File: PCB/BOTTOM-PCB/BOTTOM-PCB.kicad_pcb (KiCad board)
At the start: 2 copper layers, 61 x 61 mm, 8 parts, among them J1 Conn_01x10_Pin, J2 Conn_01x03_Pin, J3 Conn_01x02_Pin, U1 MLX90393SLW-ABA-011-RE

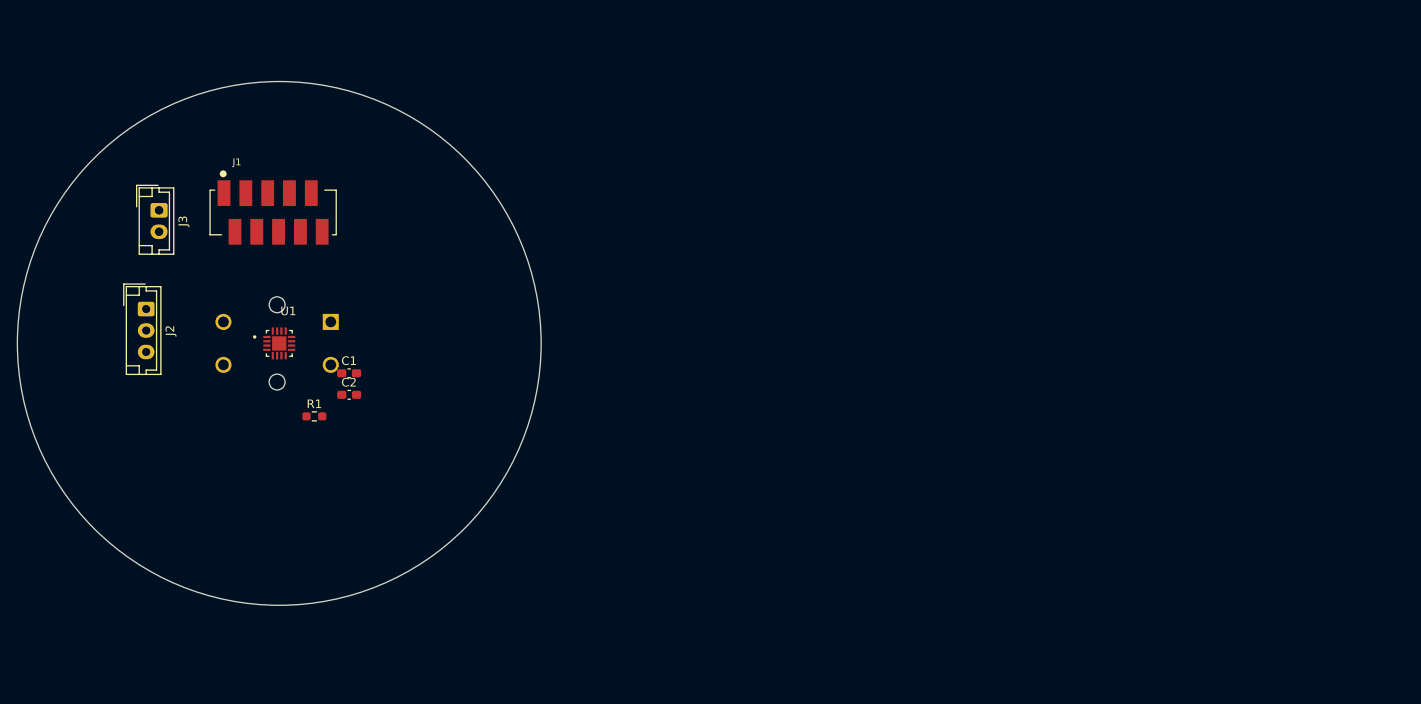
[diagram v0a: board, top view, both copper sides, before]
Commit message: re organization of top and bottom pcb
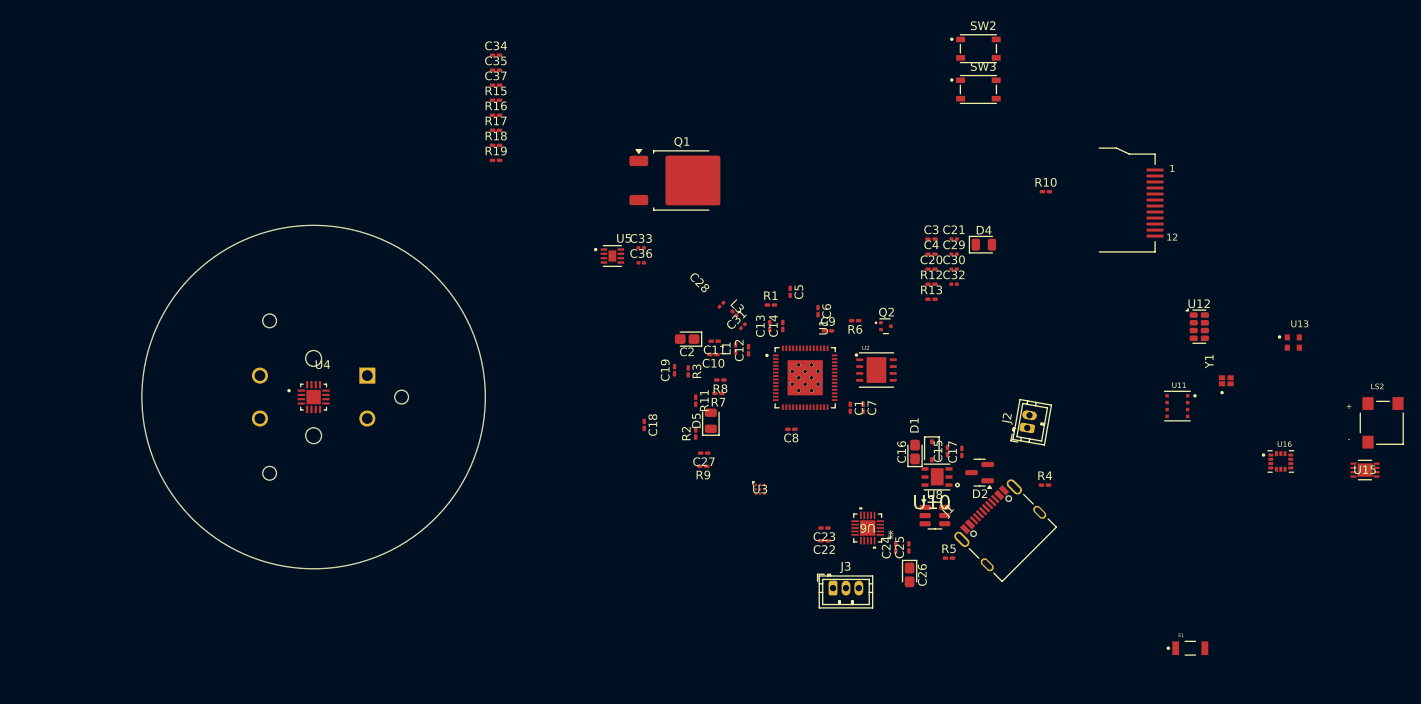
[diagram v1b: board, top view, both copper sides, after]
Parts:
- added C10: 0.1 uF, Capacitor_SMD:C_0201_0603Metric_Pad0.64x0.40mm_HandSolder, F.Cu at (189.1, 79.8)
- added C11: 1 uF, Capacitor_SMD:C_0201_0603Metric_Pad0.64x0.40mm_HandSolder, F.Cu at (189.2, 78.2)
- added C12: 0.1 uF, Capacitor_SMD:C_0201_0603Metric_Pad0.64x0.40mm_HandSolder, F.Cu at (193.2, 79.3)
- added C13: 10 nF, Capacitor_SMD:C_0201_0603Metric_Pad0.64x0.40mm_HandSolder, F.Cu at (195.6, 76.5)
- added C14: 1 uF, Capacitor_SMD:C_0201_0603Metric_Pad0.64x0.40mm_HandSolder, F.Cu at (197.1, 76.5)
- added C15: 1 uF, Capacitor_SMD:C_0201_0603Metric_Pad0.64x0.40mm_HandSolder, F.Cu at (216.3, 91.0)
- added C16: 10 uF, Capacitor_Tantalum_SMD:CP_EIA-1608-08_AVX-J_HandSolder, F.Cu at (212.5, 91.1)
- added C17: 1 uF, Capacitor_SMD:C_0201_0603Metric_Pad0.64x0.40mm_HandSolder, F.Cu at (218.0, 91.1)
- added C18: 0.1 uF, Capacitor_SMD:C_0201_0603Metric_Pad0.64x0.40mm_HandSolder, F.Cu at (181.0, 88.0)
- added C19: 0.1 uF, Capacitor_SMD:C_0201_0603Metric_Pad0.64x0.40mm_HandSolder, F.Cu at (184.5, 81.6)
- added C20: 0.1 uF, Capacitor_SMD:C_0201_0603Metric_Pad0.64x0.40mm_HandSolder, F.Cu at (214.5, 69.9)
- added C21: 1 uF, Capacitor_SMD:C_0201_0603Metric, F.Cu at (217.1, 66.4)
- added C22: 0.1 uF, Capacitor_SMD:C_0201_0603Metric_Pad0.64x0.40mm_HandSolder, F.Cu at (202.0, 101.5)
- added C23: 0.1 uF, Capacitor_SMD:C_0201_0603Metric_Pad0.64x0.40mm_HandSolder, F.Cu at (202.0, 100.0)
- added C24: 0.1 uF, Capacitor_SMD:C_0201_0603Metric_Pad0.64x0.40mm_HandSolder, F.Cu at (210.3, 102.3)
- added C25: 0.1 uF, Capacitor_SMD:C_0201_0603Metric_Pad0.64x0.40mm_HandSolder, F.Cu at (211.8, 102.3)
- added C26: 22 uF, Capacitor_Tantalum_SMD:CP_EIA-1608-08_AVX-J_HandSolder, F.Cu at (211.9, 105.5)
- added C27: 0.1 uF, Capacitor_SMD:C_0201_0603Metric_Pad0.64x0.40mm_HandSolder, F.Cu at (188.0, 91.3)
- added C28: 1.8 pF, Capacitor_SMD:C_0201_0603Metric, F.Cu at (190.0, 74.0)
- added C29: 1 uF, Capacitor_SMD:C_0201_0603Metric, F.Cu at (217.1, 68.1)
- added C3: 0.1 uF, Capacitor_SMD:C_0201_0603Metric_Pad0.64x0.40mm_HandSolder, F.Cu at (214.5, 66.4)
- added C30: 4.7 uF, Capacitor_SMD:C_0201_0603Metric, F.Cu at (217.1, 69.9)
- added C31: 1.5 pF, Capacitor_SMD:C_0201_0603Metric, F.Cu at (192.5, 76.5)
- added C32: 4.7 uF, Capacitor_SMD:C_0201_0603Metric, F.Cu at (217.1, 71.6)
- added C33: 0.1 uF, Capacitor_SMD:C_0201_0603Metric, F.Cu at (180.7, 67.4)
- added C34: 0.1 uF, Capacitor_SMD:C_0201_0603Metric_Pad0.64x0.40mm_HandSolder, F.Cu at (163.7, 44.9)
- added C35: 22 uF, Capacitor_SMD:C_0201_0603Metric_Pad0.64x0.40mm_HandSolder, F.Cu at (163.7, 46.7)
- added C36: 0.1 uF, Capacitor_SMD:C_0201_0603Metric, F.Cu at (180.7, 69.1)
- added C37: 0.1 uF, Capacitor_SMD:C_0201_0603Metric_Pad0.64x0.40mm_HandSolder, F.Cu at (163.7, 48.4)
- added C4: 0.1 uF, Capacitor_SMD:C_0201_0603Metric_Pad0.64x0.40mm_HandSolder, F.Cu at (214.5, 68.1)
- added C5: 6 pF, Capacitor_SMD:C_0201_0603Metric_Pad0.64x0.40mm_HandSolder, F.Cu at (198.0, 72.5)
- added C6: 6 pF, Capacitor_SMD:C_0201_0603Metric_Pad0.64x0.40mm_HandSolder, F.Cu at (201.2, 74.7)
- added C7: 0.1 uF, Capacitor_SMD:C_0201_0603Metric_Pad0.64x0.40mm_HandSolder, F.Cu at (206.5, 86.0)
- added C8: 0.1 uF, Capacitor_SMD:C_0201_0603Metric_Pad0.64x0.40mm_HandSolder, F.Cu at (198.1, 88.5)
- added C9: 0.1 uF, Capacitor_SMD:C_0201_0603Metric_Pad0.64x0.40mm_HandSolder, F.Cu at (202.4, 77.0)
- added D1: SD03_SOD323, Diode_SMD:D_SOD-323, F.Cu at (214.5, 91.0)
- added D2: BAT54C, Package_TO_SOT_SMD:SOT-23, F.Cu at (220.1, 93.5)
- added D4: LED, LED_SMD:LED_0805_2012Metric, F.Cu at (220.6, 67.0)
- added D5: LED, LED_SMD:LED_0805_2012Metric, F.Cu at (188.8, 87.5)
- added E1: AMCA31-2R450G-S1F-T3, AMCA31_2R450G_S1F_T3:XDCR_AMCA31-2R450G-S1F-T3, F.Cu at (244.6, 114.0)
- added J5: Conn_01x12_Pin, GC9A01:GC9A01Round1.28, F.Cu at (240.5, 62.1)
- added L1: 2.0 nH, Inductor_SMD:L_0201_0603Metric_Pad0.64x0.40mm_HandSolder, F.Cu at (191.7, 79.1)
- added L3: 3.9 nH, Inductor_SMD:L_0201_0603Metric, F.Cu at (191.5, 75.0)
- added LS2: CMT-0525-75-SMT-TR, CMT_0525_75_SMT_TR:XDCR_CMT-0525-75-SMT-TR, F.Cu at (266.9, 87.8)
- added Q1: QM6006D, Package_TO_SOT_SMD:TO-252-2, F.Cu at (185.4, 59.5)
- added Q2: NPN, Package_TO_SOT_SMD:SOT-723, F.Cu at (209.2, 76.5)
- added R10: 10 K, Resistor_SMD:R_0201_0603Metric_Pad0.64x0.40mm_HandSolder, F.Cu at (227.8, 60.8)
- added R11: 220, Resistor_SMD:R_0201_0603Metric_Pad0.64x0.40mm_HandSolder, F.Cu at (187.0, 85.2)
- added R12: 470, Resistor_SMD:R_0201_0603Metric_Pad0.64x0.40mm_HandSolder, F.Cu at (214.5, 71.6)
- added R13: 2k, Resistor_SMD:R_0201_0603Metric_Pad0.64x0.40mm_HandSolder, F.Cu at (214.5, 73.4)
- added R15: 10 K, Resistor_SMD:R_0201_0603Metric_Pad0.64x0.40mm_HandSolder, F.Cu at (163.7, 50.2)
- added R16: 10 K, Resistor_SMD:R_0201_0603Metric_Pad0.64x0.40mm_HandSolder, F.Cu at (163.7, 51.9)
- added R17: 1 M, Resistor_SMD:R_0201_0603Metric_Pad0.64x0.40mm_HandSolder, F.Cu at (163.7, 53.7)
- added R18: 22R, Resistor_SMD:R_0201_0603Metric_Pad0.64x0.40mm_HandSolder, F.Cu at (163.7, 55.4)
- added R19: 5 K, Resistor_SMD:R_0201_0603Metric_Pad0.64x0.40mm_HandSolder, F.Cu at (163.7, 57.2)
- added R2: 5 K, Resistor_SMD:R_0201_0603Metric_Pad0.64x0.40mm_HandSolder, F.Cu at (187.0, 89.0)
- added R3: 5 K, Resistor_SMD:R_0201_0603Metric_Pad0.64x0.40mm_HandSolder, F.Cu at (186.1, 81.8)
- added R4: 5 K, Resistor_SMD:R_0201_0603Metric_Pad0.64x0.40mm_HandSolder, F.Cu at (227.7, 95.0)
- added R5: 5 K, Resistor_SMD:R_0201_0603Metric_Pad0.64x0.40mm_HandSolder, F.Cu at (216.5, 103.5)
- added R6: 5 K, Resistor_SMD:R_0201_0603Metric_Pad0.64x0.40mm_HandSolder, F.Cu at (205.6, 75.9)
- added R7: 10 K, Resistor_SMD:R_0201_0603Metric_Pad0.64x0.40mm_HandSolder, F.Cu at (189.6, 84.3)
- added R8: 10 K, Resistor_SMD:R_0201_0603Metric_Pad0.64x0.40mm_HandSolder, F.Cu at (189.9, 82.8)
- added R9: 10 K, Resistor_SMD:R_0201_0603Metric_Pad0.64x0.40mm_HandSolder, F.Cu at (187.9, 92.8)
- added SW2: PTS810_SJM_250_SMTR_LFS, PTS810SJM250SMTR_LFS:SW_PTS810_SJM_250_SMTR_LFS, F.Cu at (219.9, 44.2)
- added SW3: PTS810_SJM_250_SMTR_LFS, PTS810SJM250SMTR_LFS:SW_PTS810_SJM_250_SMTR_LFS, F.Cu at (219.9, 48.9)
- added U10: LP38691SD-3.3, LP38691SD_3_3_NOPB:DFN300X300X80-7N, F.Cu at (215.1, 94.1)
- added U11: BME688, BME688:IC_BME688, F.Cu at (243.1, 85.8)
- added U12: RV-3028-C7_32.768KHZ_1PPM-TA-QC, Package_SON:MicroCrystal_C7_SON-8_1.5x3.2mm_P0.9mm, F.Cu at (245.7, 76.5)
- added U13: LTR-329ALS-01, LTR_329ALS_01:IC_LTR-329ALS-01, F.Cu at (256.6, 78.4)
- added U15: MCP73832T-2ACI/MC, MCP73832T:DFN8_2x3MC_MCH-L, F.Cu at (265.0, 93.2)
- added U16: LSM6DSO32TR, LSM6DSO32TR:XDCR_LSM6DSO32TR, F.Cu at (255.1, 92.2)
- added U2: MX25R6435FZAIH0, MX25R6435FZAIH0:SON80P400X400X60-9N, F.Cu at (208.1, 81.6)
- added U3: DRV2605LYZFR, DRV2605LYZFR:YZF0009ADAD, F.Cu at (194.5, 95.5)
- added U4: MLX90393SLW-ABA-011-RE, MLX90393SLW_ABA_011_RE:QFN50P300X300X100-17N, F.Cu at (142.5, 84.8)
- added U5: MAX17048G_T10, MAX17048G_T10:SON50P200X200X80-9N, F.Cu at (177.3, 68.3)
- added U6: TMC6300-LA-T, tcm6300:21-100586_K2033&plus_1C_ADI-M, F.Cu at (207.0, 100.0)
- added U8: USBLC6-2SC6, Package_TO_SOT_SMD:SOT-23-6, F.Cu at (214.9, 98.5)
- added Y1: ABM12W-40.0000MHZ-8-B1U-T3, ABM12W_40_0000MHZ_8_B1U_T3:XTAL_ABM12W-40.0000MHZ-8-B1U-T3, F.Cu at (248.8, 82.8)
- C1: value 0.1uF -> 1 uF; footprint Capacitor_SMD:C_0603_1608Metric_Pad1.08x0.95mm_HandSolder -> Capacitor_SMD:C_0201_0603Metric_Pad0.64x0.40mm_HandSolder
- C2: value 0.1uF -> 10 uF; footprint Capacitor_SMD:C_0603_1608Metric_Pad1.08x0.95mm_HandSolder -> Capacitor_Tantalum_SMD:CP_EIA-1608-08_AVX-J_HandSolder
- J1: value Conn_01x10_Pin -> 12402012E212A; footprint 8_188275_0:TE_8-188275-0 -> 12402012E212A:AMPHENOL_12402012E212A
- J2: value Conn_01x03_Pin -> S2B-PH-K-SLFSN; footprint Connector_JST:JST_EH_B3B-EH-A_1x03_P2.50mm_Vertical -> Connector_JST:JST_ZH_B2B-ZR_1x02_P1.50mm_Vertical
- J3: value Conn_01x02_Pin -> Conn_01x03_Pin; footprint Connector_JST:JST_EH_B2B-EH-A_1x02_P2.50mm_Vertical -> Connector_JST:JST_ZH_B3B-ZR_1x03_P1.50mm_Vertical
- R1: value 5K -> 0; footprint Resistor_SMD:R_0603_1608Metric_Pad0.98x0.95mm_HandSolder -> Resistor_SMD:R_0201_0603Metric_Pad0.64x0.40mm_HandSolder
- U1: value MLX90393SLW-ABA-011-RE -> ESP32-S3; footprint MLX90393SLW_ABA_011_RE:QFN50P300X300X100-17N -> ESP32_S3:IC_ESP32-S3
- moved J2 103.5 mm to (225.6, 88.3), turned to 80 degrees
- moved J1 94.2 mm to (224.0, 101.2), turned to 45 degrees
- moved J3 90.0 mm to (203.0, 107.0), turned to 0 degrees
- moved U1 61.4 mm to (199.8, 82.5)
- moved C1 58.5 mm to (205.0, 86.0), turned to -90 degrees
- moved R1 54.7 mm to (195.7, 74.0)
- moved C2 39.9 mm to (186.0, 78.0), turned to 180 degrees
- moved S1 7.56 mm to (142.5, 84.8)
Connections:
- C1 pad 1: USR_BUTT -> VDD_SPI
- C2 pad 1: +3V3 -> +3.3V
- J2 pad 1: U -> +BATT
- J2 pad 2: V -> GND
- J3 pad 1: GND -> U
- J3 pad 2: +BATT -> V
- R1 pad 1: +3V3 -> Net-(C5-Pad2)
- R1 pad 2: USR_BUTT -> XTAL_P
- U1 pad 1: GND -> LNA_IN
- U1 pad 10: unconnected-(U1-N/C__2-Pad10) -> Haptic
- U1 pad 11: GND -> VL
- U1 pad 12: GND -> WL
- U1 pad 13: GND -> UL
- U1 pad 14: unconnected-(U1-N/C__3-Pad14) -> WH
- U1 pad 15: +3V3 -> VH
- U1 pad 16: unconnected-(U1-N/C__4-Pad16) -> UH
- U1 pad 17: unconnected-(U1-EXP-Pad17) -> DIAG
- U1 pad 2: ENCODER -> +3.3VA
- U1 pad 3: SCLK -> +3.3VA
- U1 pad 4: unconnected-(U1-N/C-Pad4) -> Reset
- U1 pad 5: DO -> Boot
- U1 pad 6: DO -> LED
- U1 pad 7: GND -> SCL
- U1 pad 8: +3V3 -> SDA
- U1 pad 9: unconnected-(U1-N/C__1-Pad9) -> MFP
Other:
- board size 61 x 61 mm -> 40 x 40 mm

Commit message: start routing on bottom pcb
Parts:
- removed C34: 0.1 uF, Capacitor_SMD:C_0201_0603Metric_Pad0.64x0.40mm_HandSolder
- removed C35: 22 uF, Capacitor_SMD:C_0201_0603Metric_Pad0.64x0.40mm_HandSolder
- removed Q1: QM6006D, Package_TO_SOT_SMD:TO-252-2
- removed R16: 10 K, Resistor_SMD:R_0201_0603Metric_Pad0.64x0.40mm_HandSolder
- removed R17: 1 M, Resistor_SMD:R_0201_0603Metric_Pad0.64x0.40mm_HandSolder
- removed R18: 22R, Resistor_SMD:R_0201_0603Metric_Pad0.64x0.40mm_HandSolder
- added J4: Conn_01x04_Pin, Connector_PinHeader_1.27mm:PinHeader_1x04_P1.27mm_Vertical, F.Cu at (164.2, 63.2)
- J5: value Conn_01x12_Pin -> Conn_01x04_Pin; footprint GC9A01:GC9A01Round1.28 -> Connector_PinHeader_1.27mm:PinHeader_1x04_P1.27mm_Vertical
- moved LS2 125.2 mm to (142.3, 74.8)
- moved U12 121.5 mm to (124.7, 87.9), turned to 180 degrees
- moved Y1 112.1 mm to (136.9, 89.5), turned to 0 degrees
- moved U15 111.1 mm to (154.1, 85.5)
- moved U16 110.1 mm to (145.8, 79.6)
- moved R10 107.2 mm to (125.0, 91.4), turned to 90 degrees
- moved SW2 101.3 mm to (135.2, 99.6), turned to 90 degrees
- moved U13 100.7 mm to (156.1, 72.9)
- moved U11 93.1 mm to (151.3, 70.3)
- moved SW3 86.3 mm to (150.0, 99.5), turned to 90 degrees
- moved R4 83.4 mm to (144.2, 96.3), turned to 90 degrees
- moved U6 82.0 mm to (128.4, 76.7)
- moved J1 81.5 mm to (142.5, 102.9), turned to 0 degrees
- moved C7 79.6 mm to (127.3, 93.5), turned to 180 degrees
- moved U2 78.9 mm to (130.4, 95.9), turned to 90 degrees
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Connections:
- J5 pad 1: GND -> nCS
- J5 pad 2: LEDK -> SCLK
- J5 pad 3: LEDA -> MOSI
- J5 pad 4: +3.3V -> nRESET
- U1 pad 22: unconnected-(U1-XTAL_32K_N-Pad22) -> RTC
- U1 pad 23: 17 -> EVI
- U12 pad 1: CLK -> RTC_CLK
- U4 pad 5: DO -> MOSI
- U4 pad 6: DO -> MISO
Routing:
- net +3.3V: track 0.00 -> 32.4 mm, vias 0 -> 4
- net USB_DP: track 0.00 -> 19.4 mm, vias 0 -> 2
- net USB_DN: track 0.00 -> 19.3 mm, vias 0 -> 2
- net LNA_IN: track 0.00 -> 17.7 mm
- net +5VA: track 0.00 -> 16.2 mm
- net SPI_WP: track 0.00 -> 9.32 mm, vias 0 -> 2
- net +BATT: track 0.00 -> 8.92 mm
- net RTC: track 0.00 -> 8.47 mm, vias 0 -> 2
- net USB_DN1: track 0.00 -> 7.23 mm
- net SPI_CS0: track 0.00 -> 7.01 mm, vias 0 -> 2
- net SPI_Q: track 0.00 -> 6.95 mm, vias 0 -> 2
- net USB_DP1: track 0.00 -> 6.84 mm
- net XTAL_N: track 0.00 -> 6.80 mm
- net SCL: track 0.00 -> 6.72 mm, vias 0 -> 2
- net VS: track 0.00 -> 6.68 mm
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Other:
- copper layers 2 -> 4

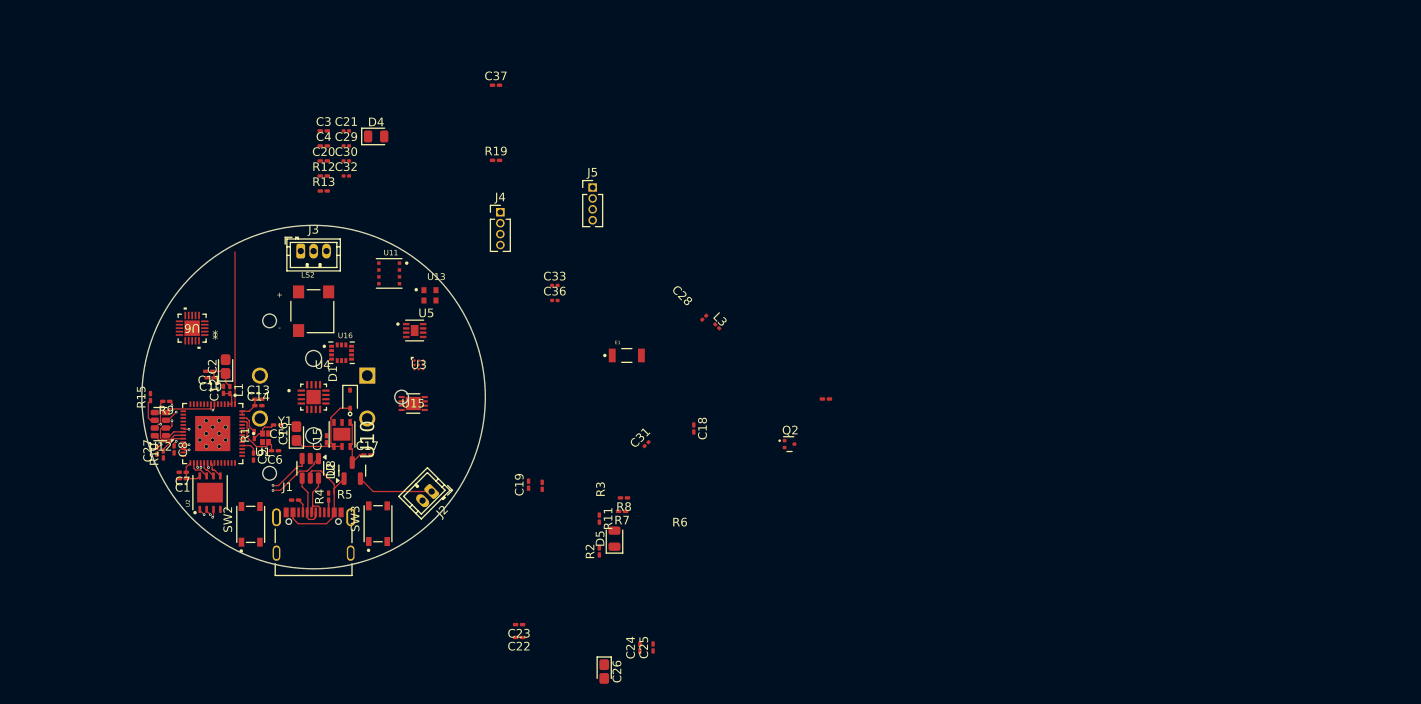
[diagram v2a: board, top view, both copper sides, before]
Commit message: connections for bottom pcb
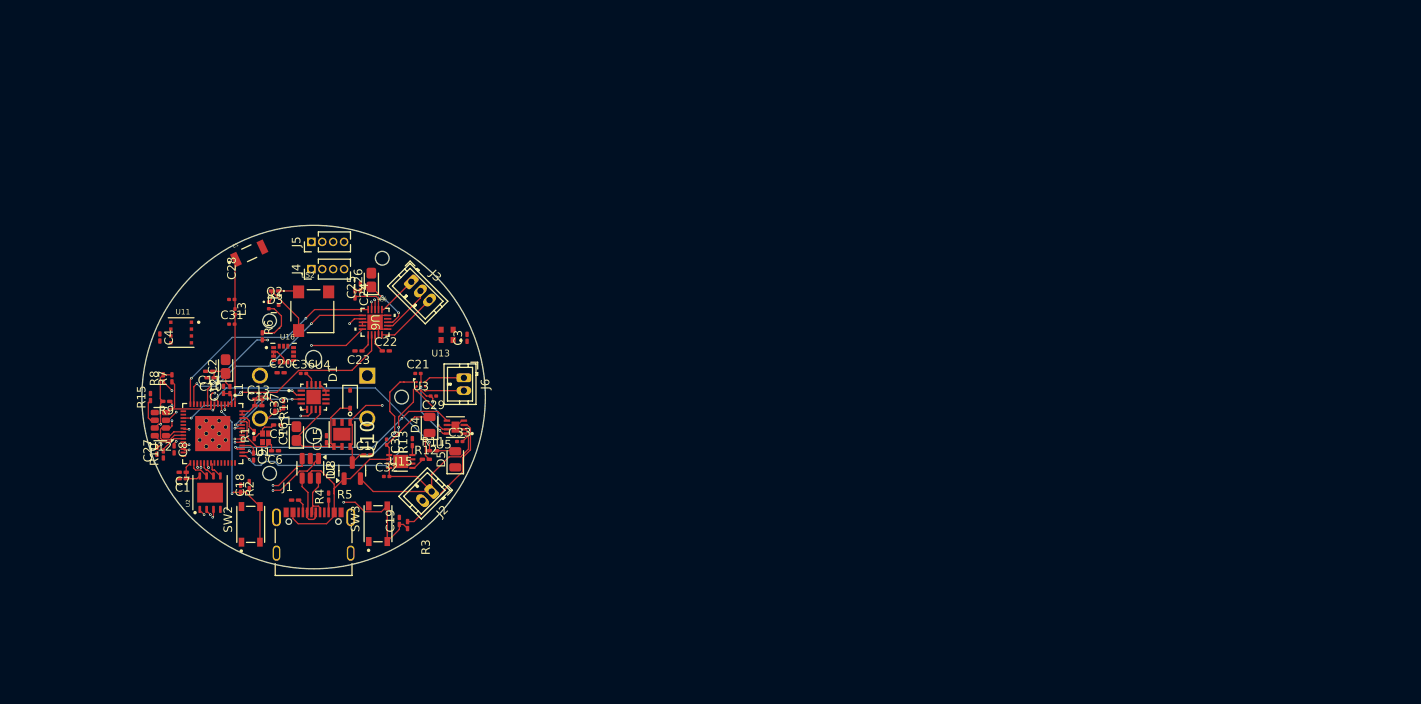
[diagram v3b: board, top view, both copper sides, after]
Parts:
- added D3: D, Diode_SMD:D_0201_0603Metric_Pad0.64x0.40mm_HandSolder, F.Cu at (138.0, 72.4)
- added J6: Conn_01x02_Pin, Connector_JST:JST_ZH_B2B-ZR_1x02_P1.50mm_Vertical, F.Cu at (160.0, 82.5)
- moved R6 66.0 mm to (136.5, 77.7), turned to -90 degrees
- moved Q2 62.2 mm to (137.9, 74.1)
- moved L3 56.2 mm to (133.3, 74.8), turned to -90 degrees
- moved R8 55.4 mm to (125.0, 82.6), turned to 90 degrees
- moved C28 55.1 mm to (133.0, 73.4), turned to 0 degrees
- moved R7 54.7 mm to (126.0, 82.6), turned to 90 degrees
- moved C25 54.1 mm to (148.0, 72.0)
- moved C26 53.1 mm to (149.2, 71.1), turned to 90 degrees
- moved C24 52.9 mm to (147.3, 72.8), turned to -90 degrees
- moved C18 52.2 mm to (135.0, 95.0), turned to 90 degrees
- moved C31 50.3 mm to (133.0, 76.3), turned to 0 degrees
- moved E1 45.6 mm to (135.0, 68.0), turned to 25 degrees
- moved C37 44.6 mm to (139.0, 85.6), turned to 90 degrees
- moved R2 42.4 mm to (134.0, 95.4), turned to -90 degrees
- moved R19 38.6 mm to (138.0, 86.0), turned to -90 degrees
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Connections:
- net VS renamed +5V
- J3 pad 1: U -> W
- J3 pad 3: W -> U
- SW2 pad 1: unconnected-(SW2-Pad1) -> GND
- SW2 pad 4: unconnected-(SW2-Pad4) -> Boot
- SW3 pad 1: unconnected-(SW3-Pad1) -> GND
- SW3 pad 4: unconnected-(SW3-Pad4) -> Reset
- U1 pad 10: Haptic -> unconnected-(U1-GPIO5-Pad10)
- U1 pad 18: Buzzer -> unconnected-(U1-GPIO13-Pad18)
- U1 pad 43: 38 -> Haptic_trigg
- U1 pad 44: 39 -> Haptic
- U1 pad 45: 40 -> Gauge
- U1 pad 47: 41 -> MISO
- U1 pad 48: 42 -> MOSI
- U1 pad 51: 45 -> SCLK
- U1 pad 52: 46 -> ENCODER
- U1 pad 9: MFP -> Buzzer
- U15 pad 3: +BAT1 -> +BATT
- U15 pad 4: +BAT1 -> +BATT
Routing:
- net SCL: track 6.72 -> 47.7 mm, vias 2 -> 5
- net SDA: track 5.93 -> 46.0 mm, vias 0 -> 3
- net +3.3V: track 32.4 -> 65.8 mm
- net Reset: track 0.00 -> 32.7 mm, vias 0 -> 2
- net LED: track 0.00 -> 29.9 mm, vias 0 -> 2
- net Haptic_trigg: track 0.00 -> 28.3 mm, vias 0 -> 2
- net Haptic: track 0.00 -> 27.7 mm, vias 0 -> 2
- net Gauge: track 0.00 -> 27.7 mm, vias 0 -> 2
- net DIAG: track 0.00 -> 27.0 mm, vias 0 -> 2
- net WH: track 0.00 -> 27.0 mm, vias 0 -> 2
- net UL: track 0.00 -> 25.4 mm, vias 0 -> 2
- net +5V: track 6.68 -> 28.4 mm, vias 0 -> 4
- net Boot: track 0.00 -> 20.3 mm, vias 0 -> 2
- net +BATT: track 8.92 -> 27.6 mm
- net GND: track 0.00 -> 17.4 mm
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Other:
- outline, holes or cut-outs redrawn

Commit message: things to improve
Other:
- outline, holes or cut-outs redrawn
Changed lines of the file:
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@@
-	)
-	(gr_circle
-		(center 150.495 68.58)
-		(end 151.295 68.58)
-		(stroke
-			(width 0.05)
-			(type solid)
-		)
-		(fill no)
-		(layer "Edge.Cuts")
 	)
 	(gr_circle

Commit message: I think its ready again
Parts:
- removed D1: SD03_SOD323, Diode_SMD:D_SOD-323
- C1, C10, C11, C12, C13, C14, C15, C17, C18, C19, C20, C22, C23, C24, C25, C27, C3, C37, C4, C5, C6, C7, C8, C9: footprint Capacitor_SMD:C_0201_0603Metric_Pad0.64x0.40mm_HandSolder -> Capacitor_SMD:C_0402_1005Metric_Pad0.74x0.62mm_HandSolder
- C21, C29, C30, C32, C33, C36: footprint Capacitor_SMD:C_0201_0603Metric -> Capacitor_SMD:C_0402_1005Metric_Pad0.74x0.62mm_HandSolder
- C28, C31: footprint Capacitor_SMD:C_0201_0603Metric -> Capacitor_SMD:C_0201_0603Metric_Pad0.64x0.40mm_HandSolder
- D3: footprint Diode_SMD:D_0201_0603Metric_Pad0.64x0.40mm_HandSolder -> Diode_SMD:D_0402_1005Metric_Pad0.77x0.64mm_HandSolder
- L1: footprint Inductor_SMD:L_0201_0603Metric_Pad0.64x0.40mm_HandSolder -> Inductor_SMD:L_0402_1005Metric_Pad0.77x0.64mm_HandSolder
- L3: footprint Inductor_SMD:L_0201_0603Metric -> Inductor_SMD:L_0201_0603Metric_Pad0.64x0.40mm_HandSolder
- R1, R10, R11, R12, R13, R15, R19, R2, R3, R4, R5, R6, R7, R8, R9: footprint Resistor_SMD:R_0201_0603Metric_Pad0.64x0.40mm_HandSolder -> Resistor_SMD:R_0402_1005Metric_Pad0.72x0.64mm_HandSolder
- moved R5 4.10 mm to (141.2, 92.8), turned to 180 degrees
- moved U8 2.87 mm to (140.3, 95.3), turned to 0 degrees
- moved R10 1.52 mm to (124.1, 90.2)
- moved C18 1.32 mm to (136.2, 95.4)
- moved C27 1.19 mm to (125.1, 90.2)
- moved R15 1.00 mm to (123.5, 83.8)
- moved U12 0.94 mm to (124.8, 87.0)
- moved C10 0.93 mm to (129.6, 82.5)
- moved R9 0.88 mm to (125.2, 84.4)
- moved R2 0.83 mm to (134.6, 96.0), turned to 0 degrees
- moved C11 0.82 mm to (129.6, 81.5)
- moved C12 0.72 mm to (131.3, 83.6)
- moved C8 0.71 mm to (126.0, 90.2)
- moved C26 0.64 mm to (149.7, 71.6)
- moved C2 0.59 mm to (132.0, 80.6)
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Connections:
- U1 pad 27: 21 -> unconnected-(U1-GPIO21-Pad27)
- U1 pad 36: 48 -> INT2
- U1 pad 37: 47 -> INT1
- U1 pad 38: 33 -> unconnected-(U1-GPIO33-Pad38)
- U1 pad 39: 34 -> DC
- U1 pad 40: 35 -> BACKLIGHT_EN
- U1 pad 41: 36 -> nCS
- U1 pad 42: 37 -> nRESET
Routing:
- net +3.3V: track 65.8 -> 172.3 mm, vias 4 -> 33
- net GND: track 17.4 -> 86.8 mm, vias 0 -> 356
- net nRESET: track 0.00 -> 49.3 mm, vias 0 -> 2
- net DC: track 0.00 -> 43.8 mm, vias 0 -> 2
- net nCS: track 0.00 -> 36.3 mm, vias 0 -> 1
- net UH: track 1.17 -> 34.8 mm, vias 1 -> 2
- net VH: track 0.91 -> 32.2 mm, vias 1 -> 2
- net BACKLIGHT_EN: track 0.00 -> 28.0 mm, vias 0 -> 2
- net MOSI: track 10.9 -> 35.4 mm, vias 2 -> 3
- net WL: track 1.73 -> 24.0 mm, vias 1 -> 2
- net SCL: track 47.7 -> 69.0 mm, vias 5 -> 6
- net SDA: track 46.0 -> 67.2 mm, vias 3 -> 7
- net SCLK: track 9.99 -> 29.5 mm, vias 2 -> 3
- net INT2: track 0.00 -> 19.1 mm, vias 0 -> 2
- net VL: track 6.73 -> 22.8 mm, vias 1 -> 2
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- added copper zone on B.Cu, net GND
- added copper zone on F.Cu, net GND
- added copper zone on In1.Cu, net GND
- added copper zone on In2.Cu, net GND
